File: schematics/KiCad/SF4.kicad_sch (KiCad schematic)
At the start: 31 parts, among them J1 Power, J2 Digital/PWM, J3 Analog, J4 Digital/PWM, J5 AudioJack2, J6 AudioJack2, U1 TL072, U2 LM358, U3 MCP6002-xP, U6 VTL5C

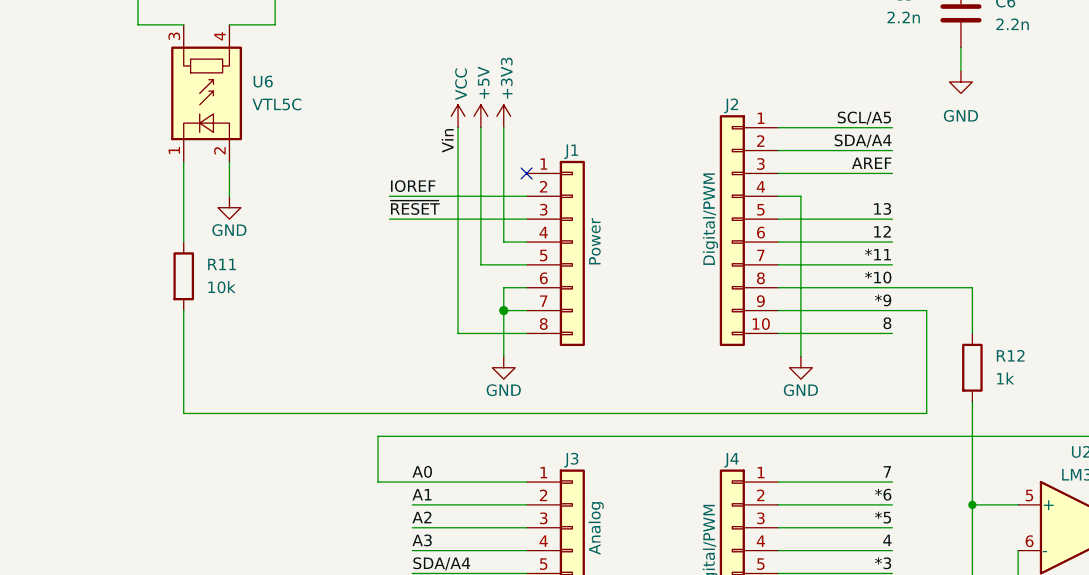
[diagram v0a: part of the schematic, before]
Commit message: audio output stage edited
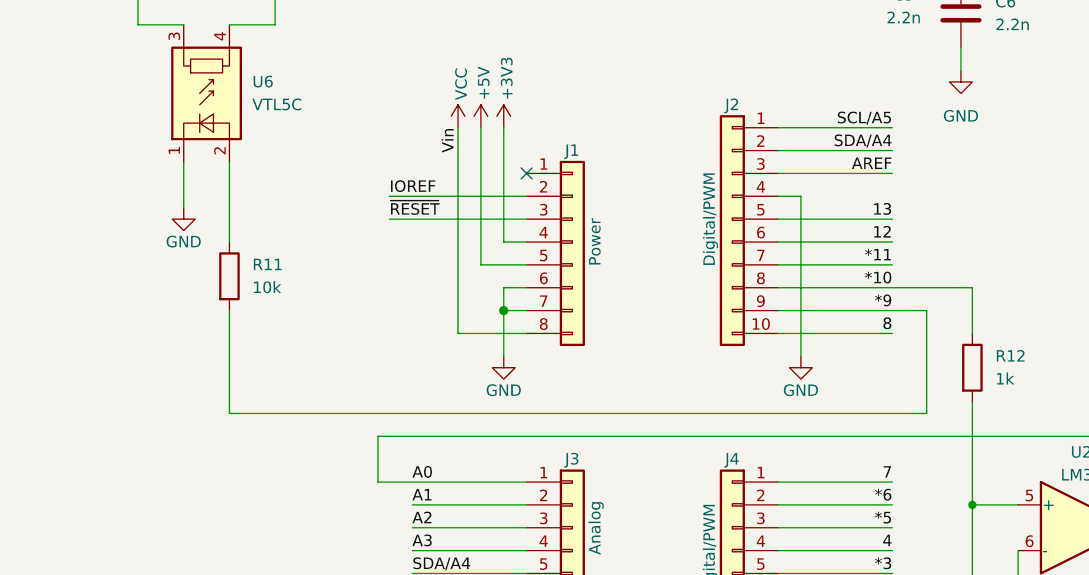
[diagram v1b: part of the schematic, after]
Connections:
- net GND: now also U6.1 (-); no longer U6.2 (+)
- net at R11.1: now also U6.2 (+); no longer U6.1 (-)
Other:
- moved on the sheet: R11
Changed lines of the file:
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@@
 	(wire
 		(pts
-			(xy 135.89 100.33) (xy 135.89 91.44)
+			(xy 140.97 91.44) (xy 140.97 100.33)
 		)
 		(stroke
@@
 	(wire
 		(pts
-			(xy 218.44 119.38) (xy 135.89 119.38)
+			(xy 218.44 119.38) (xy 140.97 119.38)
 		)
 		(stroke
@@
 	(wire
 		(pts
+			(xy 135.89 91.44) (xy 135.89 96.52)
+		)
+		(stroke
+			(width 0)
+			(type default)
+		)
+	)
+	(wire
+		(pts
 			(xy 86.36 71.12) (xy 86.36 74.93)
 		)
@@
 	(wire
 		(pts
-			(xy 140.97 91.44) (xy 140.97 95.25)
-		)
-		(stroke
-			(width 0)
-			(type default)
-		)
-	)
-	(wire
-		(pts
 			(xy 242.57 121.92) (xy 242.57 68.58)
 		)
@@
 	(wire
 		(pts
-			(xy 135.89 119.38) (xy 135.89 107.95)
+			(xy 140.97 119.38) (xy 140.97 107.95)
 		)
 		(stroke
@@
 	(symbol
 		(lib_id "Device:R")
-		(at 135.89 104.14 0)
+		(at 140.97 104.14 0)
 		(unit 1)
 		(body_style 1)
@@
 		(fields_autoplaced yes)
 		(property "Reference" "R11"
-			(at 138.43 102.8699 0)
+			(at 143.51 102.8699 0)
 			(show_name no)
 			(do_not_autoplace no)
@@
 		)
 		(property "Value" "10k"
-			(at 138.43 105.4099 0)
+			(at 143.51 105.4099 0)
 			(show_name no)
 			(do_not_autoplace no)
@@
 		)
 		(property "Footprint" ""
-			(at 134.112 104.14 90)
+			(at 139.192 104.14 90)
 			(hide yes)
 			(show_name no)
@@
 		)
 		(property "Datasheet" ""
-			(at 135.89 104.14 0)
+			(at 140.97 104.14 0)
 			(hide yes)
 			(show_name no)
@@
 		)
 		(property "Description" "Resistor"
-			(at 135.89 104.14 0)
+			(at 140.97 104.14 0)
 			(hide yes)
 			(show_name no)
@@
 	(symbol
 		(lib_id "power:GND")
-		(at 140.97 95.25 0)
+		(at 135.89 96.52 0)
 		(unit 1)
 		(body_style 1)
@@
 		(dnp no)
 		(property "Reference" "#PWR017"
-			(at 140.97 101.6 0)
+			(at 135.89 102.87 0)
 			(hide yes)
 			(show_name no)
@@
 		)
 		(property "Value" "GND"
-			(at 140.97 99.06 0)
+			(at 135.89 100.33 0)
 			(show_name no)
 			(do_not_autoplace no)
@@
 		)
 		(property "Footprint" ""
-			(at 140.97 95.25 0)
+			(at 135.89 96.52 0)
 			(show_name no)
 			(do_not_autoplace no)
@@
 		)
 		(property "Datasheet" ""
-			(at 140.97 95.25 0)
+			(at 135.89 96.52 0)
 			(show_name no)
 			(do_not_autoplace no)
@@
 		)
 		(property "Description" "Power symbol creates a global label with name \"GND\" , ground"
-			(at 140.97 95.25 0)
+			(at 135.89 96.52 0)
 			(hide yes)
 			(show_name no)

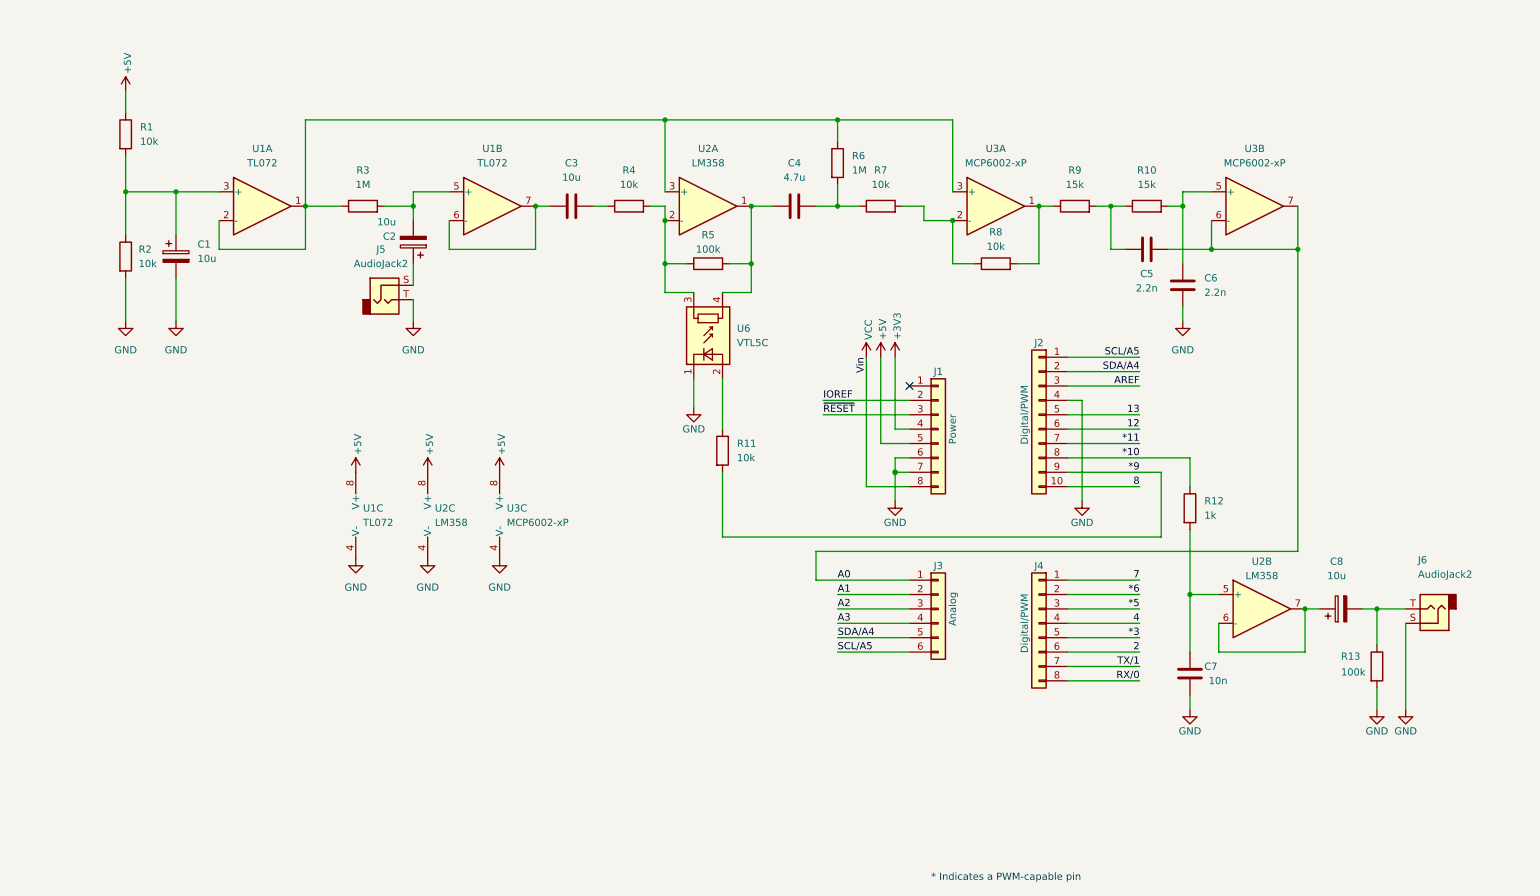
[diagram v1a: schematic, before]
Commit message: updated schematic for the output stage
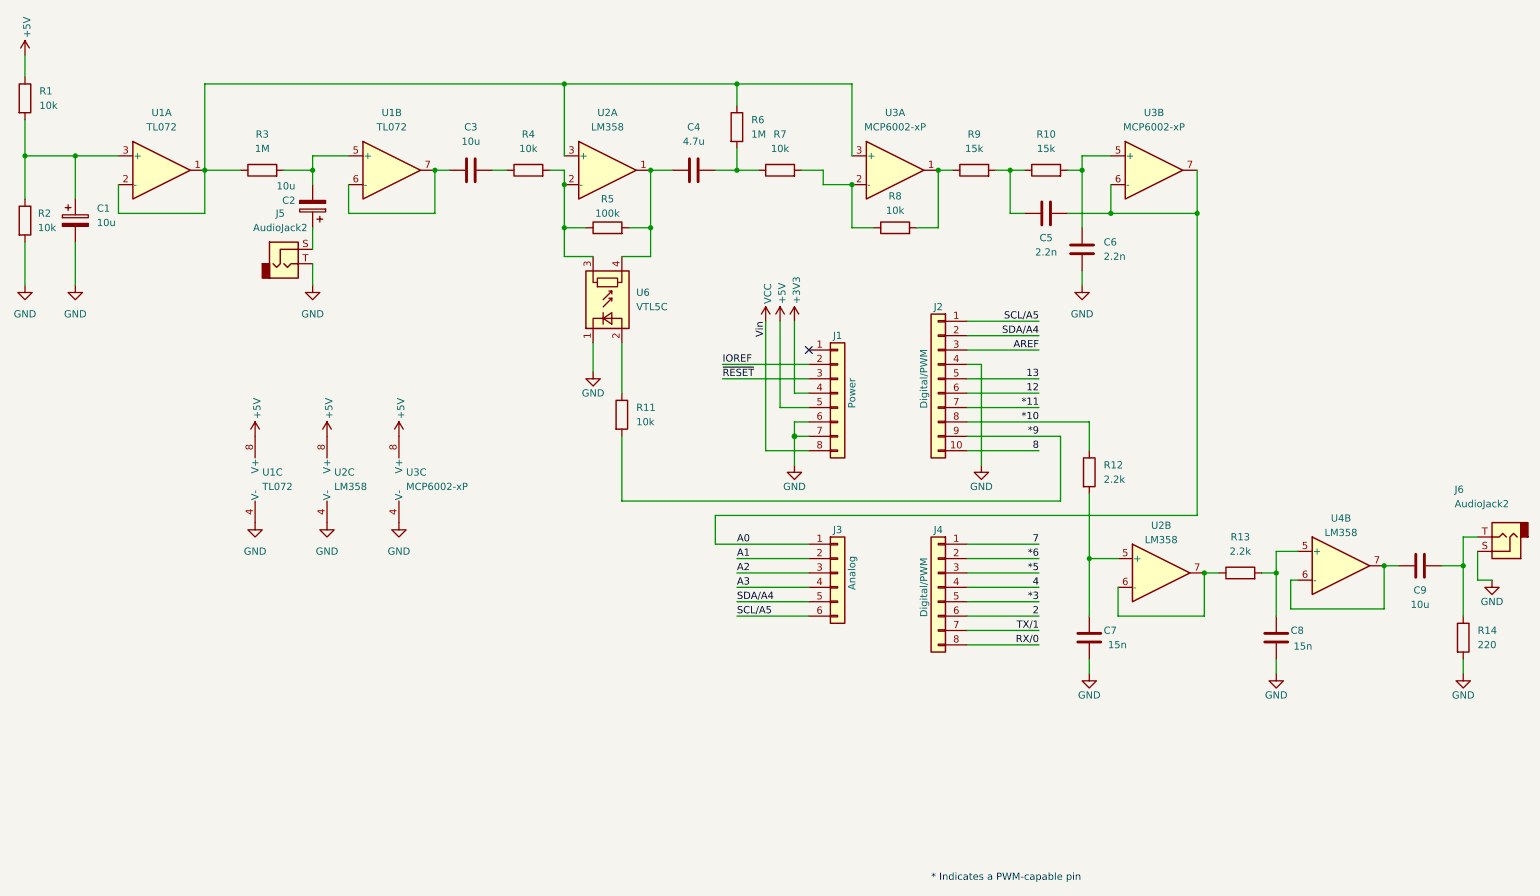
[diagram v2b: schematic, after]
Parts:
- removed C8: 10u, symbol Device:C_Polarized
- added C8: 15n, symbol Device:C
- added C9: 10u, symbol Device:C
- added R14: 220, symbol Device:R
- added U4: LM358, symbol Amplifier_Operational:LM358
- C7: value 10n -> 15n
- R12: value 1k -> 2.2k
- R13: value 100k -> 2.2k
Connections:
- net GND: now also C8.2, R14.2; no longer R13.2
- net at R13.1: now also U2.6 (-), U2.7; no longer J6.T
- new net: C8.1, R13.2, U4.5 (+)
- new net: C9.1, U4.6 (-), U4.7
- new net: C9.2, J6.T, R14.1
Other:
- moved on the sheet: C1, C2, C3, C4, C5, C6, C7, J1, J2, J3, J4, J5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
